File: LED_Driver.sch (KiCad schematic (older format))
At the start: 6 parts

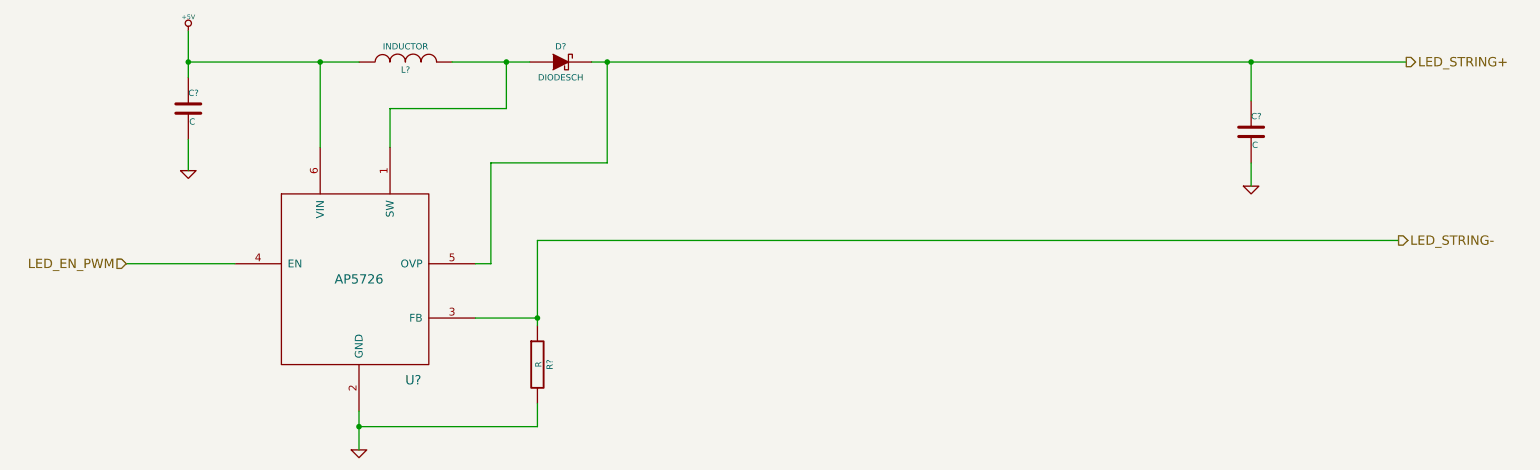
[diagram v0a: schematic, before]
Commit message: Created Footprints and Placed Relay Module
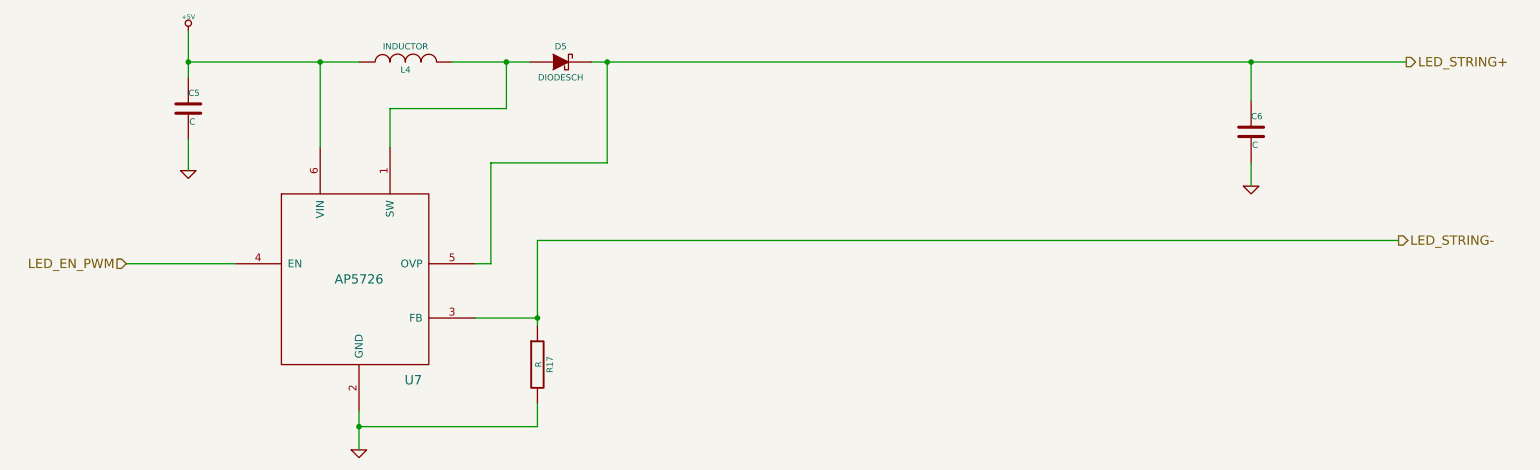
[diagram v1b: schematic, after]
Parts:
- gave numbers to parts that had none: 6
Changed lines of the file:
@@
-EESchema Schematic File Version 2  date 10/10/2013 12:18:22 AM
+EESchema Schematic File Version 2  date 10/10/2013 1:06:29 AM
 LIBS:power
 LIBS:device
@@
 LED_STRING+
 $Comp
-L AP5726 U?
+L AP5726 U7
 U 1 1 523F52C8
 P 3650 3050
-F 0 "U?" H 4000 2400 60  0000 C CNN
+F 0 "U7" H 4000 2400 60  0000 C CNN
 F 1 "AP5726" H 3650 3050 60  0000 C CNN
 F 2 "" H 3550 3150 60  0000 C CNN
@@
 	2150 2950 2850 2950
 $Comp
-L +5V #PWR?
+L +5V #PWR32
 U 1 1 523F5D4A
 P 2550 1450
-F 0 "#PWR?" H 2550 1540 20  0001 C CNN
+F 0 "#PWR32" H 2550 1540 20  0001 C CNN
 F 1 "+5V" H 2550 1540 30  0000 C CNN
 F 2 "~" H 2550 1450 60  0000 C CNN
@@
 $EndComp
 $Comp
-L GND #PWR?
+L GND #PWR33
 U 1 1 523F5D68
 P 2550 2350
-F 0 "#PWR?" H 2550 2350 30  0001 C CNN
+F 0 "#PWR33" H 2550 2350 30  0001 C CNN
 F 1 "GND" H 2550 2280 30  0001 C CNN
 F 2 "~" H 2550 2350 60  0000 C CNN
@@
 $EndComp
 $Comp
-L GND #PWR?
+L GND #PWR34
 U 1 1 523F5D75
 P 3650 4150
-F 0 "#PWR?" H 3650 4150 30  0001 C CNN
+F 0 "#PWR34" H 3650 4150 30  0001 C CNN
 F 1 "GND" H 3650 4080 30  0001 C CNN
 F 2 "~" H 3650 4150 60  0000 C CNN
@@
 	3650 4150 3650 3900
 $Comp
-L C C?
+L C C5
 U 1 1 523F5D89
 P 2550 1950
-F 0 "C?" H 2550 2050 40  0000 L CNN
+F 0 "C5" H 2550 2050 40  0000 L CNN
 F 1 "C" H 2556 1865 40  0000 L CNN
 F 2 "~" H 2588 1800 30  0000 C CNN
@@
 Connection ~ 2550 1650
 $Comp
-L C C?
+L C C6
 U 1 1 523F5DA2
 P 9400 2100
-F 0 "C?" H 9400 2200 40  0000 L CNN
+F 0 "C6" H 9400 2200 40  0000 L CNN
 F 1 "C" H 9406 2015 40  0000 L CNN
 F 2 "~" H 9438 1950 30  0000 C CNN
@@
 $EndComp
 $Comp
-L INDUCTOR L?
+L INDUCTOR L4
 U 1 1 523F5DAA
 P 3950 1650
-F 0 "L?" V 3900 1650 40  0000 C CNN
+F 0 "L4" V 3900 1650 40  0000 C CNN
 F 1 "INDUCTOR" V 4050 1650 40  0000 C CNN
 F 2 "~" H 3950 1650 60  0000 C CNN
@@
 	4250 1650 4750 1650
 $Comp
-L DIODESCH D?
+L DIODESCH D5
 U 1 1 523F5DF0
 P 4950 1650
-F 0 "D?" H 4950 1750 40  0000 C CNN
+F 0 "D5" H 4950 1750 40  0000 C CNN
 F 1 "DIODESCH" H 4950 1550 40  0000 C CNN
 F 2 "~" H 4950 1650 60  0000 C CNN
@@
 	9400 1650 9400 1900
 $Comp
-L GND #PWR?
+L GND #PWR35
 U 1 1 523F5E22
 P 9400 2450
-F 0 "#PWR?" H 9400 2450 30  0001 C CNN
+F 0 "#PWR35" H 9400 2450 30  0001 C CNN
 F 1 "GND" H 9400 2380 30  0001 C CNN
 F 2 "~" H 9400 2450 60  0000 C CNN
@@
 Connection ~ 9400 1650
 $Comp
-L R R?
+L R R17
 U 1 1 523F5E65
 P 4800 3600
-F 0 "R?" V 4880 3600 40  0000 C CNN
+F 0 "R17" V 4880 3600 40  0000 C CNN
 F 1 "R" V 4807 3601 40  0000 C CNN
 F 2 "~" V 4730 3600 30  0000 C CNN
